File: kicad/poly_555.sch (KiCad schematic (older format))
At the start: 32 parts, among them U1 LM386

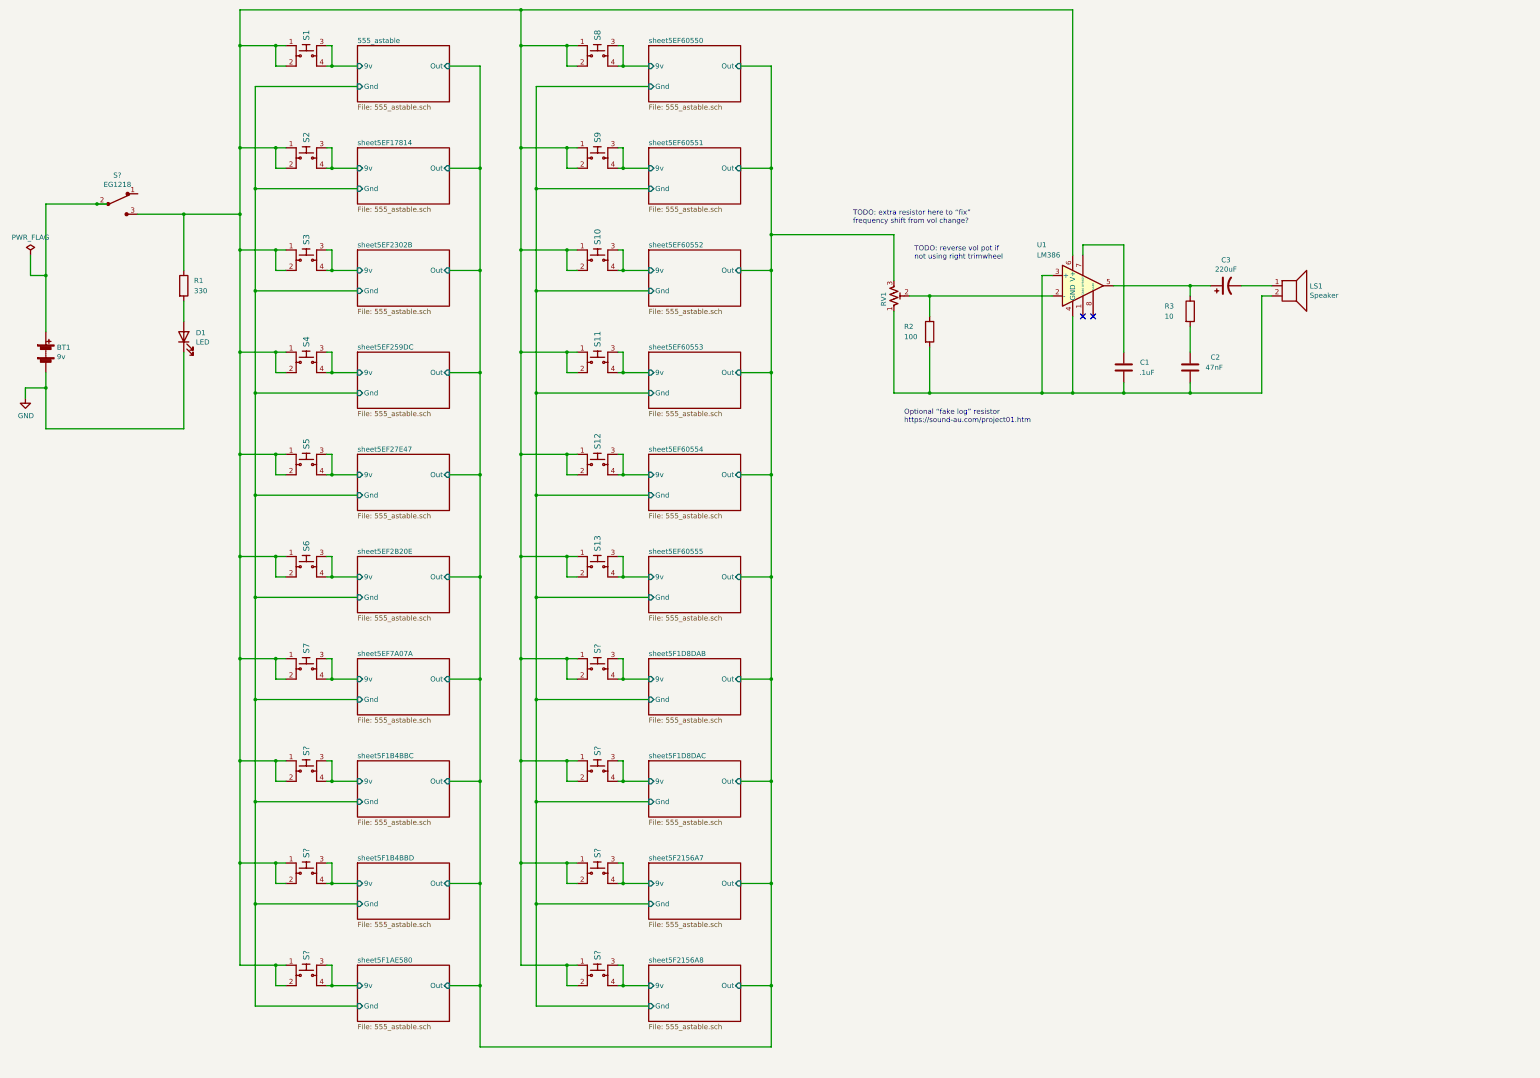
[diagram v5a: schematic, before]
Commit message: Re-annotate and update footprints
* vertical resistors
* radial, electrolytics timing caps
* add switch
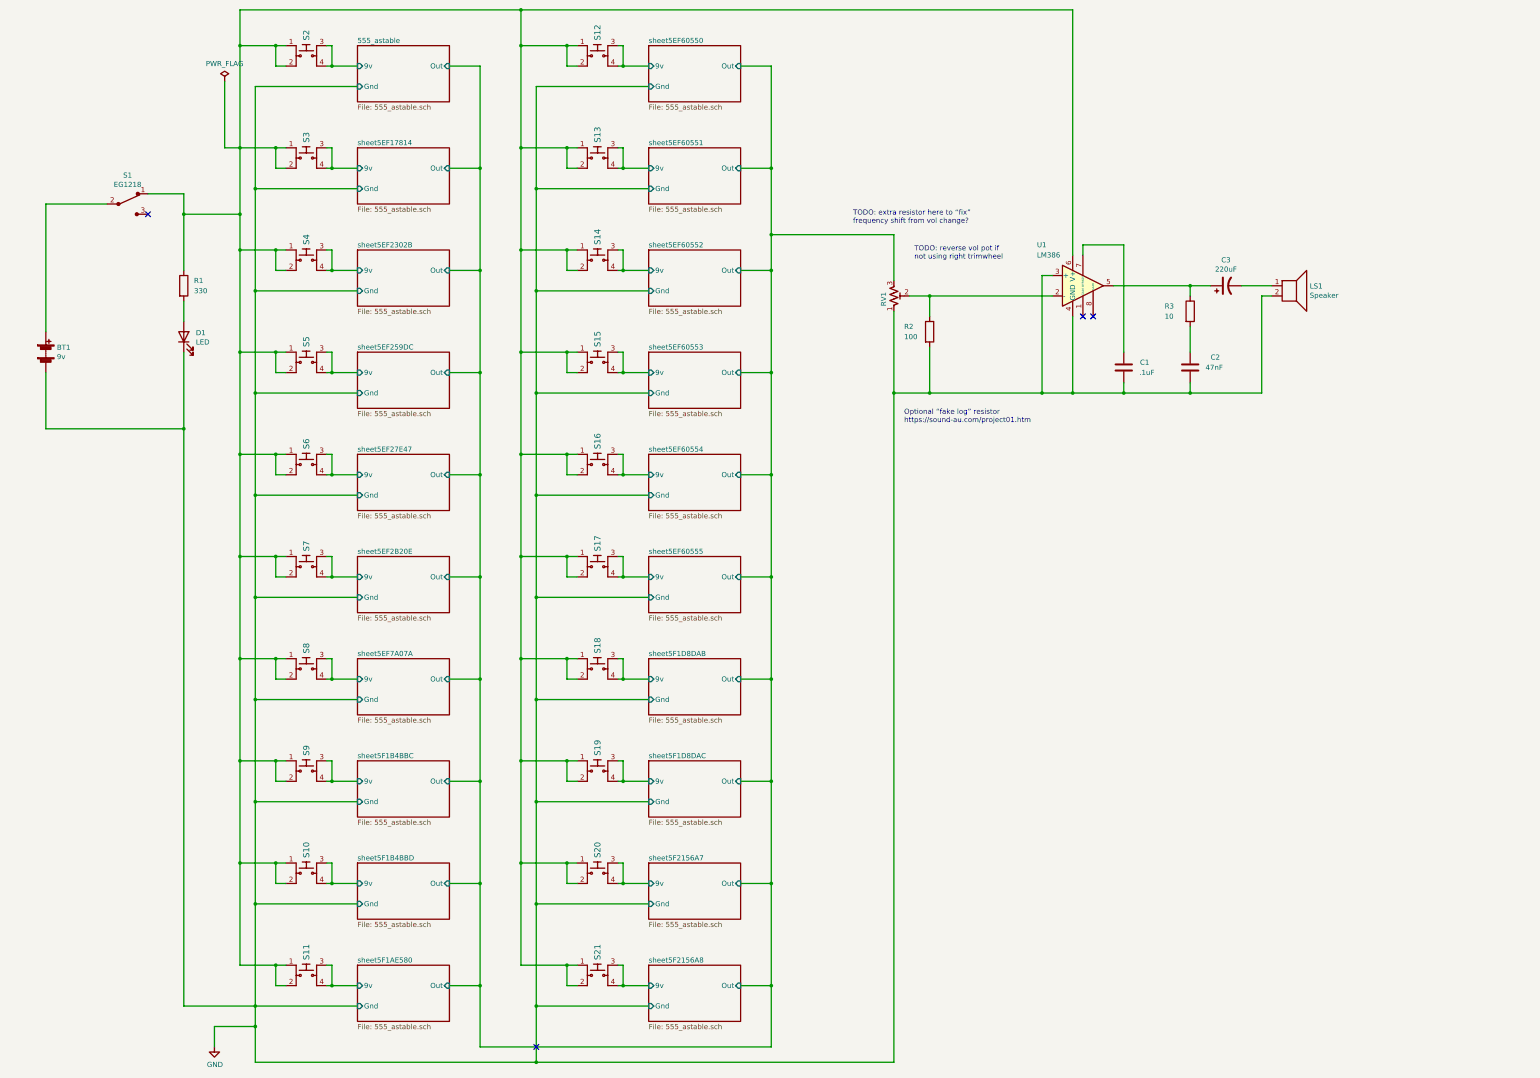
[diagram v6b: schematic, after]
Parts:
- R2, R3: footprint Resistor_THT:R_Axial_DIN0204_L3.6mm_D1.6mm_P7.62mm_Horizontal -> Resistor_THT:R_Axial_DIN0207_L6.3mm_D2.5mm_P2.54mm_Vertical
- S1: renamed from S?; footprint digikey-footprints:Switch_Slide_11.6x4mm_EG1218 -> Button_Switch_THT:SW_Slide_1P2T_CK_OS102011MS2Q
- gave numbers to parts that had none: 7
- renumbered S8 to S12, S9 to S13, S10 to S14, S11 to S15, S12 to S16, S13 to S17, S1 to S2, S2 to S3, S3 to S4, S4 to S5, S5 to S6, S6 to S7, S7 to S8
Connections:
- net GND: now also C1.1, C2.2, LS1.2, R2.2, RV1.1, U1.3 (+), U1.4 (GND)
- net at R1.1, S10.1, S10.2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: now also S1.1; no longer S1.3
- no-connect marks 2 -> 4
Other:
- moved on the sheet: S1

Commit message: Swap pot footprint
Still not the correct component that I'm using, but this one at least
has larger holes for its legs (instead of wire leads) which I'm hoping
will make the pots easier to insert
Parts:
- RV1: footprint Potentiometer_THT:Potentiometer_Bourns_3386F_Vertical -> Potentiometer_THT:Potentiometer_Piher_PT-6-V_Vertical
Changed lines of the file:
@@
 F 0 "RV1" V 9400 3600 50  0000 R CNN
 F 1 "R_POT_TRIM_US" H 9432 3455 50  0001 R CNN
-F 2 "Potentiometer_THT:Potentiometer_Bourns_3386F_Vertical" H 9500 3500 50  0001 C CNN
+F 2 "Potentiometer_THT:Potentiometer_Piher_PT-6-V_Vertical" H 9500 3500 50  0001 C CNN
 F 3 "~" H 9500 3500 50  0001 C CNN
 	1    9500 3500

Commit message: Have R2 lay flat to not obstruct a volume wheel
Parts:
- R2: footprint Resistor_THT:R_Axial_DIN0207_L6.3mm_D2.5mm_P2.54mm_Vertical -> Resistor_THT:R_Axial_DIN0207_L6.3mm_D2.5mm_P10.16mm_Horizontal
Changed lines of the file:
@@
 F 0 "R2" H 9600 3900 50  0000 L CNN
 F 1 "100" H 9600 3800 50  0000 L CNN
-F 2 "Resistor_THT:R_Axial_DIN0207_L6.3mm_D2.5mm_P2.54mm_Vertical" V 9780 3850 50  0001 C CNN
+F 2 "Resistor_THT:R_Axial_DIN0207_L6.3mm_D2.5mm_P10.16mm_Horizontal" V 9780 3850 50  0001 C CNN
 F 3 "~" H 9850 3850 50  0001 C CNN
 	1    9850 3850
